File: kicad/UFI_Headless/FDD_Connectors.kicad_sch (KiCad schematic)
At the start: 8 parts, among them J6 FDD_34PIN, J7 AMIGA_FDD

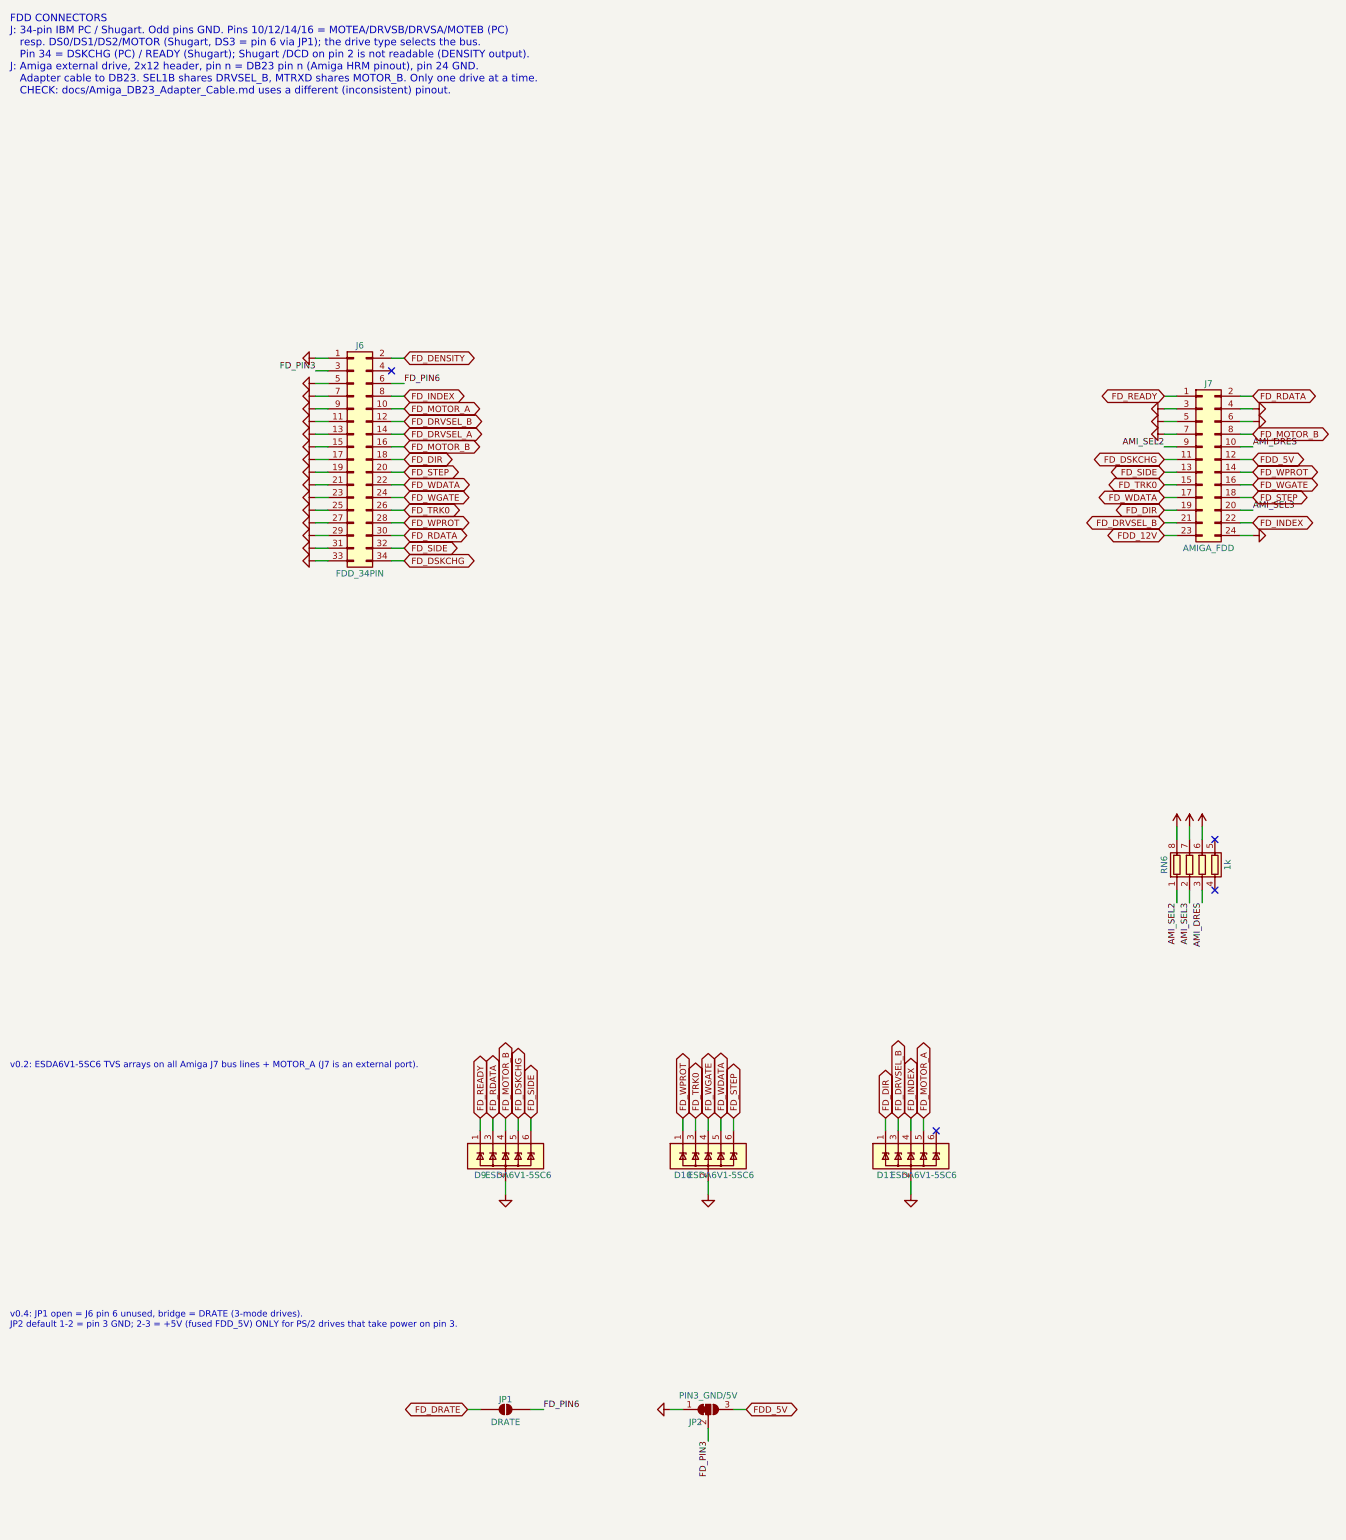
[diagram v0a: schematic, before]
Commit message: v0.7 (in progress): JP3 second Amiga drive DF2 on J7 SEL2B; firmware 1.9: drive type amiga2
- schematic: solder jumper JP3 (open) J7 pin 9 SEL2B <-> DRVSEL_A, free ESD channel of D11 on DRVSEL_A
- PCB ECO: JP3 at (67, 73), incremental Freerouting; DRC 0, unconnected 0, parity 0, via-in-pad 0
- firmware: DRIVE_AMIGA2 (10), select presents the drive's own motor state on the MTRXD latch edge
  (DF1 <-> DF2 switching keeps motors), safe state stops both latched motors; UFI.CFG drive=amiga2
- host: drive name amiga2; docs
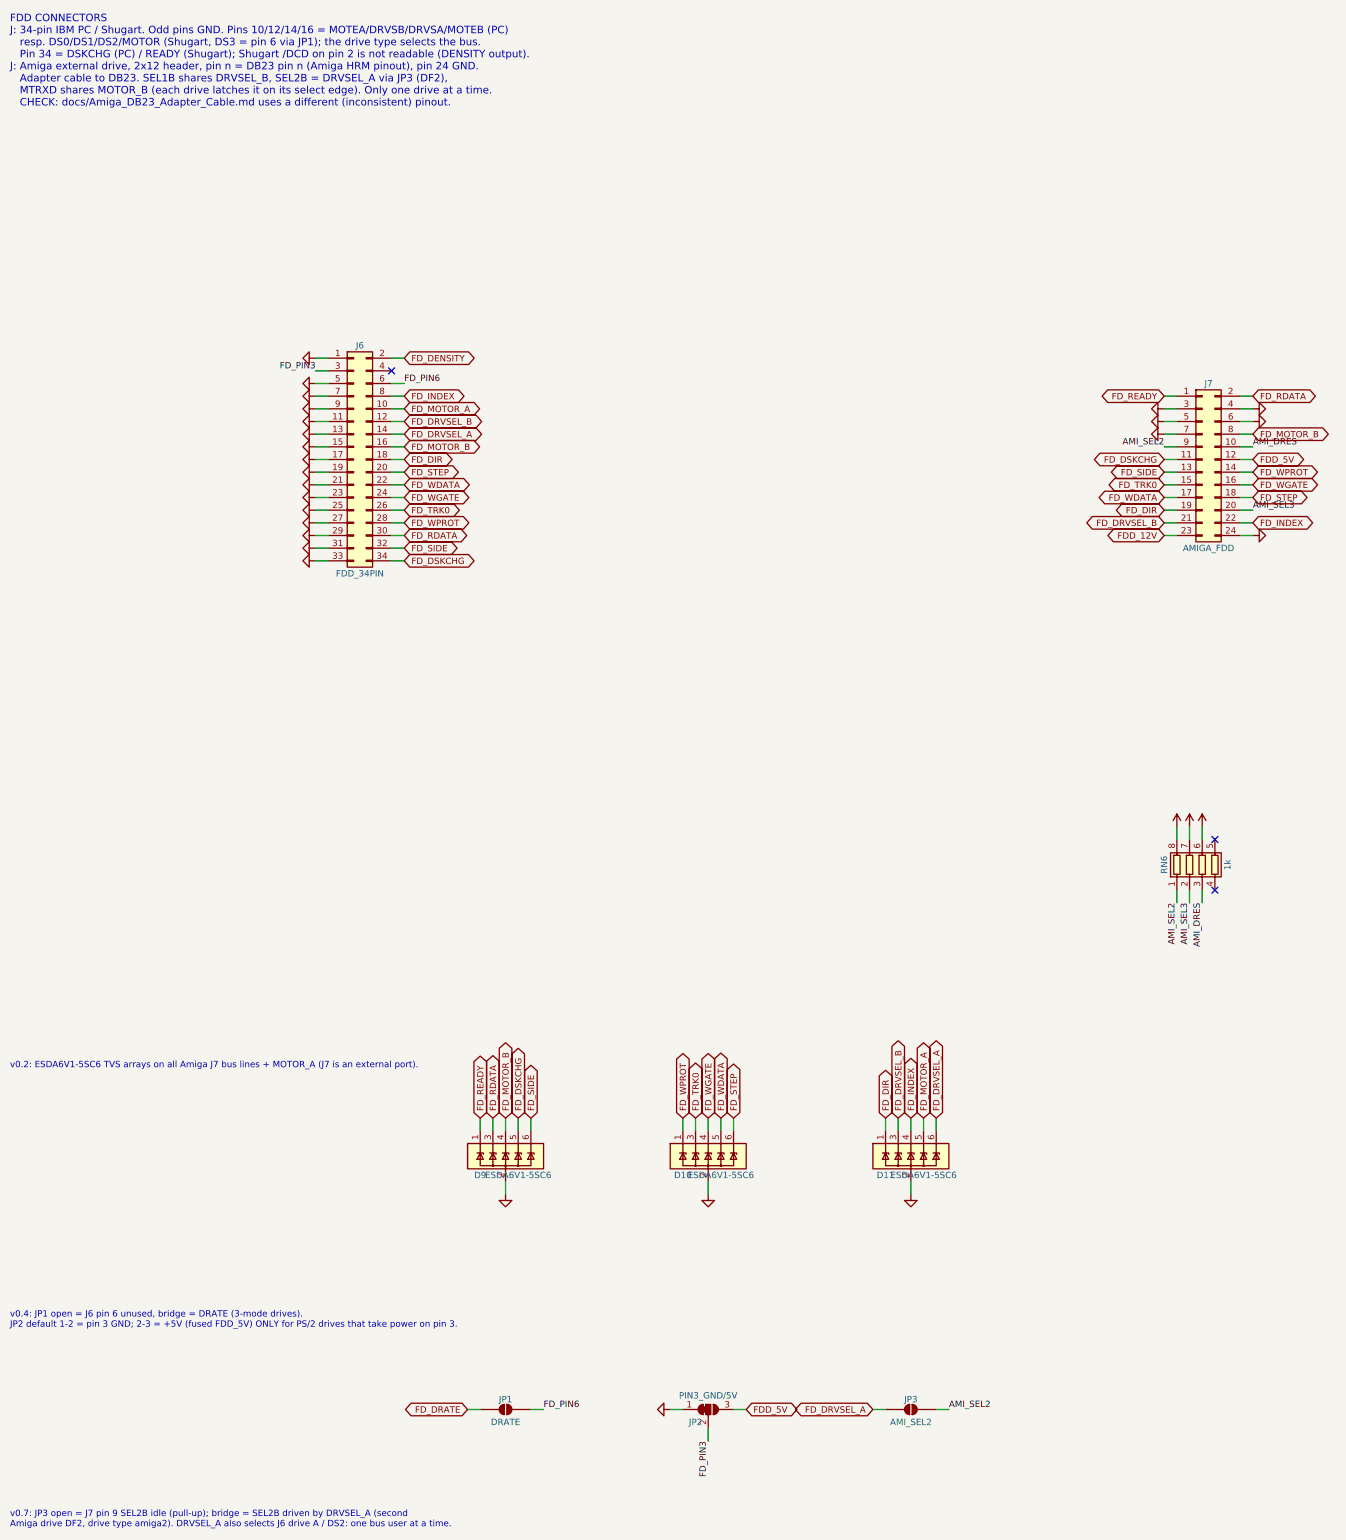
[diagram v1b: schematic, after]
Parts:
- added JP3: AMI_SEL2, Jumper:SolderJumper-2_P1.3mm_Open_RoundedPad1.0x1.5mm, symbol Jumper:SolderJumper_2_Open
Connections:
- net AMI_SEL2: now also JP3.2 (B)
- net FD_DRVSEL_A: now also D11.6 (IO5), JP3.1 (A)
- no-connect marks 4 -> 3
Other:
- note added: "v0.7: JP3 open = J7 pin 9 SEL2B idle (pull-up); bridge = SEL2B driven by DRVSEL_A (second Amiga drive DF2, drive type amiga2). DRVSEL_A also selects J6 drive A / DS2: one bus user at a time."
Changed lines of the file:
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@@
 (paper "A3")
 (title_block (title "UFI Headless - FDD Connectors") (date "2026-10-05") (rev "0.1") (company "UFI Project"))
-(text "FDD CONNECTORS\nJ: 34-pin IBM PC / Shugart. Odd pins GND. Pins 10/12/14/16 = MOTEA/DRVSB/DRVSA/MOTEB (PC)\n   resp. DS0/DS1/DS2/MOTOR (Shugart, DS3 = pin 6 via JP1); the drive type selects the bus.\n   Pin 34 = DSKCHG (PC) / READY (Shugart); Shugart /DCD on pin 2 is not readable (DENSITY output).\nJ: Amiga external drive, 2x12 header, pin n = DB23 pin n (Amiga HRM pinout), pin 24 GND.\n   Adapter cable to DB23. SEL1B shares DRVSEL_B, MTRXD shares MOTOR_B. Only one drive at a time.\n   CHECK: docs/Amiga_DB23_Adapter_Cable.md uses a different (inconsistent) pinout." (exclude_from_sim no) (at 20 20 0) (effects (font (size 1.5 1.5)) (justify left top)))
+(text "FDD CONNECTORS\nJ: 34-pin IBM PC / Shugart. Odd pins GND. Pins 10/12/14/16 = MOTEA/DRVSB/DRVSA/MOTEB (PC)\n   resp. DS0/DS1/DS2/MOTOR (Shugart, DS3 = pin 6 via JP1); the drive type selects the bus.\n   Pin 34 = DSKCHG (PC) / READY (Shugart); Shugart /DCD on pin 2 is not readable (DENSITY output).\nJ: Amiga external drive, 2x12 header, pin n = DB23 pin n (Amiga HRM pinout), pin 24 GND.\n   Adapter cable to DB23. SEL1B shares DRVSEL_B, SEL2B = DRVSEL_A via JP3 (DF2),\n   MTRXD shares MOTOR_B (each drive latches it on its select edge). Only one drive at a time.\n   CHECK: docs/Amiga_DB23_Adapter_Cable.md uses a different (inconsistent) pinout." (exclude_from_sim no) (at 20 20 0) (effects (font (size 1.5 1.5)) (justify left top)))
 (wire (pts (xy 83.82 88.9) (xy 81.28 88.9)) (stroke (width 0) (type default)))
 (wire (pts (xy 96.52 88.9) (xy 99.06 88.9)) (stroke (width 0) (type default)))
@@
 (wire (pts (xy 203.2 243.84) (xy 203.2 241.3)) (stroke (width 0) (type default)))
 (global_label "FD_MOTOR_A" (shape bidirectional) (at 203.2 241.3 90) (fields_autoplaced yes) (effects (font (size 1.27 1.27)) (justify left)) (property "Intersheetrefs" "${INTERSHEET_REFS}" (at 203.2 241.3 0) (effects (font (size 1.27 1.27)) (hide yes))))
-(no_connect (at 205.74 243.84))
+(wire (pts (xy 205.74 243.84) (xy 205.74 241.3)) (stroke (width 0) (type default)))
+(global_label "FD_DRVSEL_A" (shape bidirectional) (at 205.74 241.3 90) (fields_autoplaced yes) (effects (font (size 1.27 1.27)) (justify left)) (property "Intersheetrefs" "${INTERSHEET_REFS}" (at 205.74 241.3 0) (effects (font (size 1.27 1.27)) (hide yes))))
 (text "v0.4: JP1 open = J6 pin 6 unused, bridge = DRATE (3-mode drives).\nJP2 default 1-2 = pin 3 GND; 2-3 = +5V (fused FDD_5V) ONLY for PS/2 drives that take power on pin 3." (exclude_from_sim no) (at 20 280 0) (effects (font (size 1.27 1.27)) (justify left top)))
 (wire (pts (xy 114.3 299.72) (xy 111.76 299.72)) (stroke (width 0) (type default)))
@@
 (wire (pts (xy 165.1 299.72) (xy 167.64 299.72)) (stroke (width 0) (type default)))
 (global_label "FDD_5V" (shape bidirectional) (at 167.64 299.72 0) (fields_autoplaced yes) (effects (font (size 1.27 1.27)) (justify left)) (property "Intersheetrefs" "${INTERSHEET_REFS}" (at 167.64 299.72 0) (effects (font (size 1.27 1.27)) (hide yes))))
+(text "v0.7: JP3 open = J7 pin 9 SEL2B idle (pull-up); bridge = SEL2B driven by DRVSEL_A (second\nAmiga drive DF2, drive type amiga2). DRVSEL_A also selects J6 drive A / DS2: one bus user at a time." (exclude_from_sim no) (at 20 320 0) (effects (font (size 1.27 1.27)) (justify left top)))
+(wire (pts (xy 195.58 299.72) (xy 193.04 299.72)) (stroke (width 0) (type default)))
+(global_label "FD_DRVSEL_A" (shape bidirectional) (at 193.04 299.72 180) (fields_autoplaced yes) (effects (font (size 1.27 1.27)) (justify right)) (property "Intersheetrefs" "${INTERSHEET_REFS}" (at 193.04 299.72 0) (effects (font (size 1.27 1.27)) (hide yes))))
+(wire (pts (xy 205.74 299.72) (xy 208.28 299.72)) (stroke (width 0) (type default)))
+(label "AMI_SEL2" (at 208.28 299.72 0) (fields_autoplaced yes) (effects (font (size 1.27 1.27)) (justify left bottom)))
 (symbol (lib_id "power:GND") (at 81.28 88.9 270) (unit 1)
 (exclude_from_sim no) (in_bom no) (on_board yes) (dnp no)
@@
 (pin "3")
 (instances (project "UFI_Headless" (path "/dc1b800d-cedf-5627-97f0-e6992ff33669/7efa7110-e20d-5bc0-a817-7dc9a25f889d" (reference "JP2") (unit 1)))))
+(symbol (lib_id "Jumper:SolderJumper_2_Open") (at 200.66 299.72 0) (unit 1)
+(exclude_from_sim no) (in_bom no) (on_board yes) (dnp no)
+(property "Reference" "JP3" (at 200.66 297.688 0) (effects (font (size 1.27 1.27))))
+(property "Value" "AMI_SEL2" (at 200.66 302.26 0) (effects (font (size 1.27 1.27))))
+(property "Footprint" "Jumper:SolderJumper-2_P1.3mm_Open_RoundedPad1.0x1.5mm" (at 200.66 299.72 0) (effects (font (size 1.27 1.27)) (hide yes)))
+(property "Datasheet" "" (at 200.66 307.34 0) (effects (font (size 1.27 1.27)) (hide yes)))
+(pin "1")
+(pin "2")
+(instances (project "UFI_Headless" (path "/dc1b800d-cedf-5627-97f0-e6992ff33669/7efa7110-e20d-5bc0-a817-7dc9a25f889d" (reference "JP3") (unit 1)))))
 )

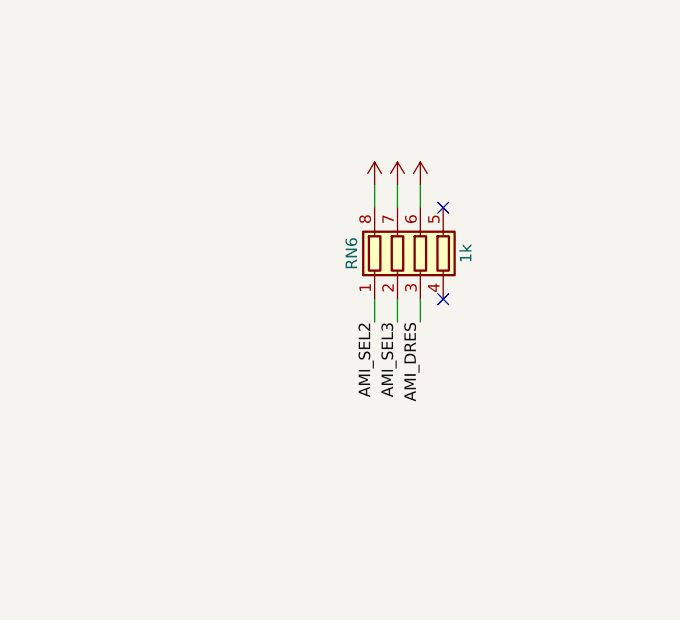
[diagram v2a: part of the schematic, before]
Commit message: KiCad v0.7 rework, schematic stages A1-A3: automatic 5 V source selection, discrete FDD termination, front-panel header - Power: J18 (5V_SEL jumper) removed, U19 TPS2116DRL selects external 5 V (J17, priority) or the 12 V buck automatically (R72 33k / R73 10k PR1 divider, C57 1 uF, status via R74 10k to +3V3 on test point TP9 TP_5V_SEL), PWR_FLAG moved to +5V_PSU_F; Flux_Interface / IEC_Bus / FDD_Connectors: RN1-RN8 (1k R_Pack04) replaced by 25 discrete 0603 1k resistors R75-R99 on the same nets (17 FDD lines, 5 IEC, 3 Amiga), array stubs, per-pin +5V symbols and orphan no-connects removed; MCU_Core: J9 EXPANSION and J13 MODE_SW removed, J12 becomes a keyed 2x8 IDC front-panel header FRONT (1 +3V3, 3 ACT, 5 ERR, 7 USB, 9 FDD, 11 PWR via R34-R37 and new R100 330 R, 13 BTN_A, 14 BTN_B, 15 MODE1, 16 MODE2 via R101-R104 470 R and TVS D18-D21, even pins 2-12 GND), on-board LEDs D5-D8 with R12-R15 removed (D4 ACT stays), SW3/SW4 marked DNP (buttons on the front); lib_symbols for Conn_02x08_Odd_Even and D_TVS added to MCU_Core; ERC over the whole project 0 errors / 0 warnings. Design brief docs/PCB_Revision_Empfehlungen_2026-10-24.md (decisions of 2026-10-24: power as before minus J18, input edge vs. drive edge, DB23 Amiga at the drive edge, W5500 LAN at the input edge, 32x 0603 termination), bring-up procedure docs/Bringup_2026-10-24.md (USB-C J1 soldered rotated 180 deg on the first board). Open for A4/A5: INDEX_SIM needs its own timer-capable MCU pin (PE1 is now the MODE2 line; firmware pin map changes in the same commit as the schematic), I2C SCL/SDA get 4 test pads, D18-D21 to be swapped for low-leakage ESD diodes (SMF3.3CA leaks up to 1 mA at 3.3 V against ~40k internal pull-ups) plus ESD on the five LED lines, +3V3 on J12 pin 1 to be fed through a 1k series resistor, loopback block, LA header, J11 slide switch, DIN-6 and DB23, W5500, then layout (USB-C edge cutout, input/output edges). Layout (.kicad_pcb) not yet touched.
Claude-Session: https://claude.ai/code/sessi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
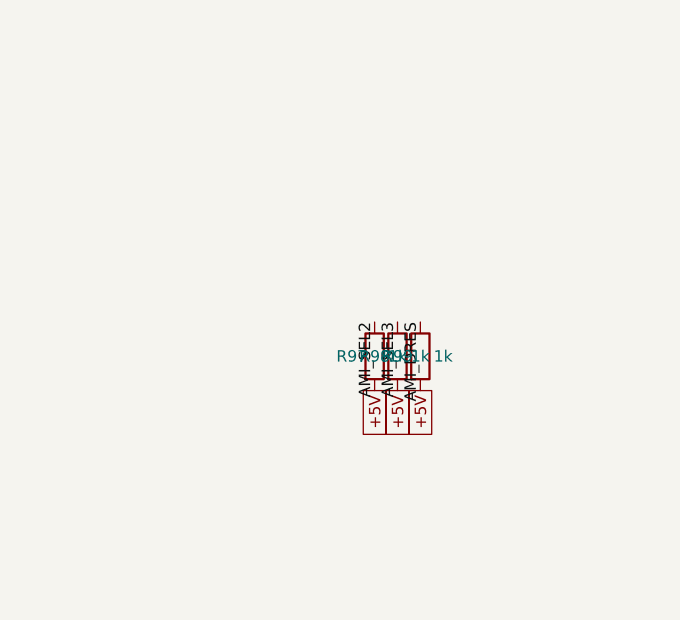
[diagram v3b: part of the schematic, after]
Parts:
- removed RN6: 1k, Resistor_SMD:R_Array_Convex_4x0603, symbol Device:R_Pack04
- added R97, R98, R99: 1k, Resistor_SMD:R_0603_1608Metric, symbol Device:R
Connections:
- net +5V: now also R97.2, R98.2, R99.2
- net AMI_DRES: now also R99.1
- net AMI_SEL2: now also R97.1
- net AMI_SEL3: now also R98.1
- no-connect marks 3 -> 1
